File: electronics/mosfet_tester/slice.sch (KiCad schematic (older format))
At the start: 18 parts, among them J201 TEST_1P, J202 TEST_1P, J203 TEST_1P, J204 TEST_1P, J205 TEST_1P, J206 TEST_1P, J207 TEST_1P, Q201 Q_NMOS_GSD, U201 LM358

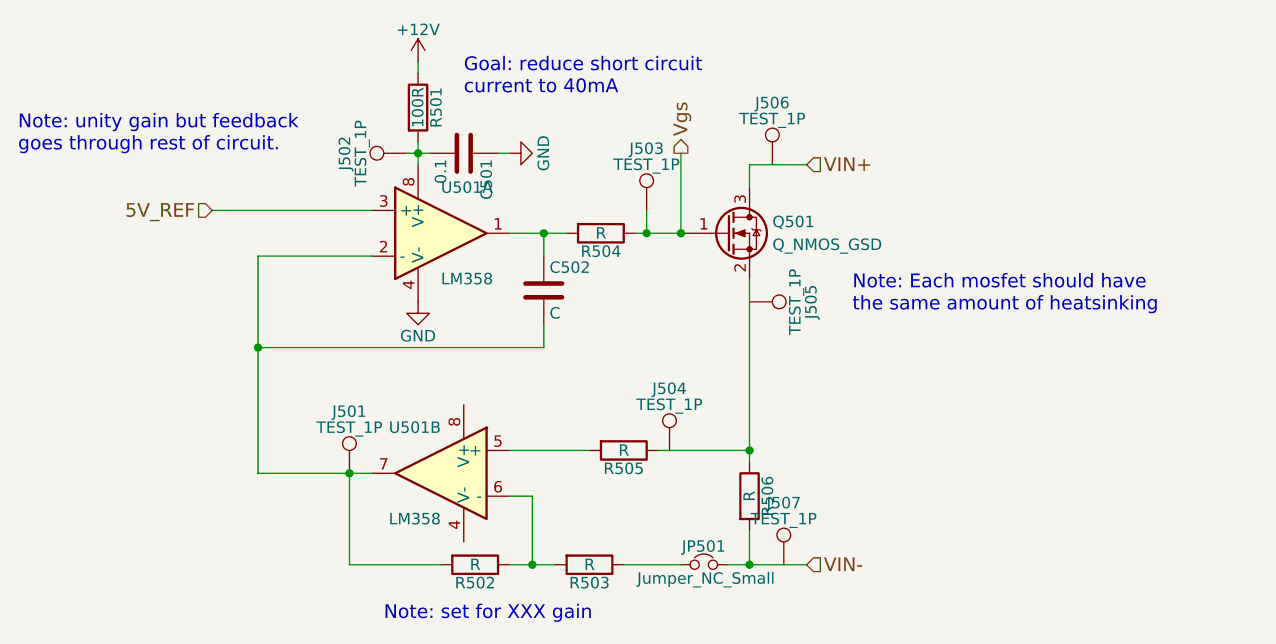
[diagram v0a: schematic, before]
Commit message: mosfet tester progress
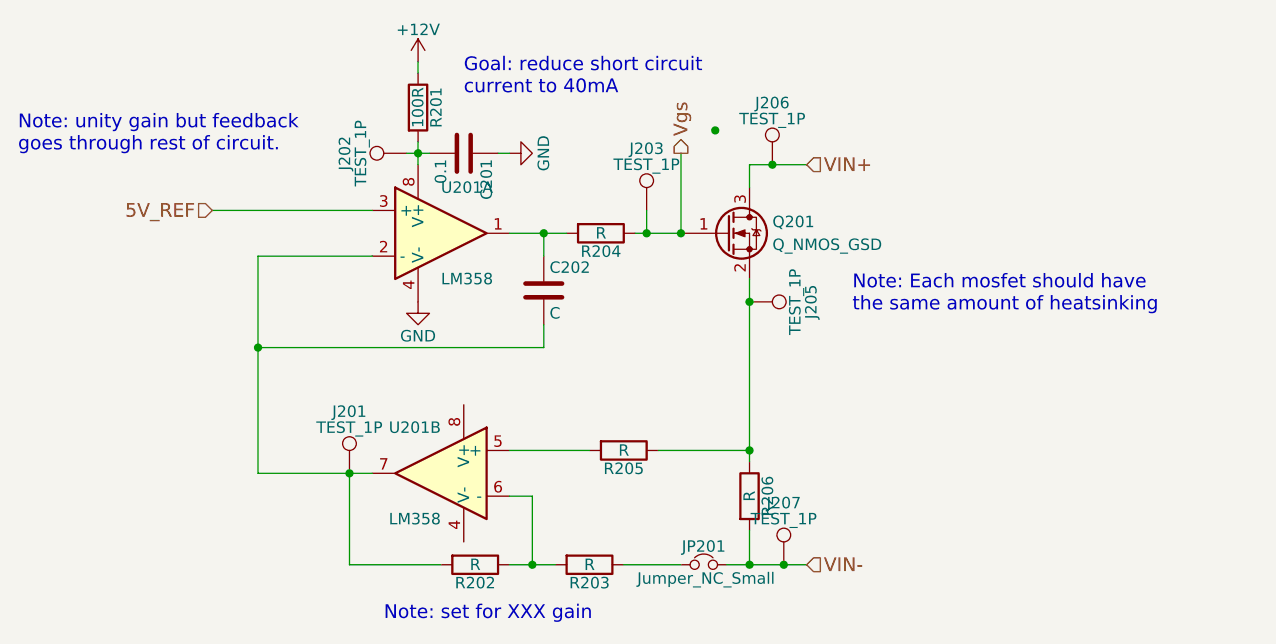
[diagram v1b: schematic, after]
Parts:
- removed J204: TEST_1P, Pin_Headers:Pin_Header_Straight_1x01_Pitch2.54mm, symbol TEST_1P
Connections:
- net VIN+: now also J206.1
- net VIN-: now also J207.1
- net at Q201.2 (S), R205.1, R206.1: now also J205.1
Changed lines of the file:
@@
 $Descr A4 11693 8268
 encoding utf-8
-Sheet 2 5
+Sheet 2 2
 Title ""
 Date ""
@@
 AR Path="/59556CE1/59553827" Ref="Q401"  Part="1"
 AR Path="/59557090/59553827" Ref="Q501"  Part="1"
-F 0 "Q501" H 4250 2350 50  0000 L CNN
+F 0 "Q201" H 4250 2350 50  0000 L CNN
 F 1 "Q_NMOS_GSD" H 4250 2250 50  0000 L CNN
 F 2 "TO_SOT_Packages_SMD:SOT-23_Handsoldering" H 4250 2400 50  0001 C CNN
@@
 AR Path="/59556CE1/5955382E" Ref="R406"  Part="1"
 AR Path="/59557090/5955382E" Ref="R506"  Part="1"
-F 0 "R506" V 4230 3450 50  0000 C CNN
+F 0 "R206" V 4230 3450 50  0000 C CNN
 F 1 "R" V 4150 3450 50  0000 C CNN
 F 2 "Resistors_SMD:R_2816_HandSoldering" V 4080 3450 50  0001 C CNN
@@
 AR Path="/59556CE1/59553867" Ref="U401"  Part="1"
 AR Path="/59557090/59553867" Ref="U501"  Part="1"
-F 0 "U501" H 2800 2500 50  0000 L CNN
+F 0 "U201" H 2800 2500 50  0000 L CNN
 F 1 "LM358" H 2800 2100 50  0000 L CNN
 F 2 "Housings_SOIC:SOIC-8_3.9x4.9mm_Pitch1.27mm" H 2800 2300 50  0001 C CNN
@@
 AR Path="/59556CE1/595538B8" Ref="U401"  Part="2"
 AR Path="/59557090/595538B8" Ref="U501"  Part="2"
-F 0 "U501" H 2800 3550 50  0000 L CNN
+F 0 "U201" H 2800 3550 50  0000 L CNN
 F 1 "LM358" H 2800 3150 50  0000 L CNN
 F 2 "Housings_SOIC:SOIC-8_3.9x4.9mm_Pitch1.27mm" H 2800 3350 50  0001 C CNN
@@
 Note: set for XXX gain
 $Comp
-L +12V #PWR201
+L +12V #PWR08
 U 1 1 59553CF4
 P 2700 1550
-AR Path="/595536CF/59553CF4" Ref="#PWR201"  Part="1"
+AR Path="/595536CF/59553CF4" Ref="#PWR08"  Part="1"
 AR Path="/59556746/59553CF4" Ref="#PWR301"  Part="1"
 AR Path="/59556CE1/59553CF4" Ref="#PWR401"  Part="1"
 AR Path="/59557090/59553CF4" Ref="#PWR501"  Part="1"
-F 0 "#PWR501" H 2700 1400 50  0001 C CNN
+F 0 "#PWR08" H 2700 1400 50  0001 C CNN
 F 1 "+12V" H 2700 1690 50  0000 C CNN
 F 2 "" H 2700 1550 50  0001 C CNN
@@
 AR Path="/59556CE1/59553D78" Ref="R401"  Part="1"
 AR Path="/59557090/59553D78" Ref="R501"  Part="1"
-F 0 "R501" V 2780 1750 50  0000 C CNN
+F 0 "R201" V 2780 1750 50  0000 C CNN
 F 1 "100R" V 2700 1750 50  0000 C CNN
 F 2 "Resistors_SMD:R_0603_HandSoldering" V 2630 1750 50  0001 C CNN
@@
 AR Path="/59556CE1/59553ED0" Ref="C401"  Part="1"
 AR Path="/59557090/59553ED0" Ref="C501"  Part="1"
-F 0 "C501" H 2925 2050 50  0000 L CNN
+F 0 "C201" H 2925 2050 50  0000 L CNN
 F 1 "0.1" H 2925 1850 50  0000 L CNN
 F 2 "Capacitors_SMD_Round:C_0603" H 2938 1800 50  0001 C CNN
@@
 	2700 1600 2700 1550
 $Comp
-L GND #PWR203
+L GND #PWR09
 U 1 1 59553F9C
 P 3100 1950
-AR Path="/595536CF/59553F9C" Ref="#PWR203"  Part="1"
+AR Path="/595536CF/59553F9C" Ref="#PWR09"  Part="1"
 AR Path="/59556746/59553F9C" Ref="#PWR303"  Part="1"
 AR Path="/59556CE1/59553F9C" Ref="#PWR403"  Part="1"
 AR Path="/59557090/59553F9C" Ref="#PWR503"  Part="1"
-F 0 "#PWR503" H 3100 1700 50  0001 C CNN
+F 0 "#PWR09" H 3100 1700 50  0001 C CNN
 F 1 "GND" H 3100 1800 50  0000 C CNN
 F 2 "" H 3100 1950 50  0001 C CNN
@@
 AR Path="/59556CE1/59554405" Ref="R405"  Part="1"
 AR Path="/59557090/59554405" Ref="R505"  Part="1"
-F 0 "R505" V 3680 3250 50  0000 C CNN
+F 0 "R205" V 3680 3250 50  0000 C CNN
 F 1 "R" V 3600 3250 50  0000 C CNN
 F 2 "Resistors_SMD:R_0603_HandSoldering" V 3530 3250 50  0001 C CNN
@@
 AR Path="/59556CE1/5955448A" Ref="R404"  Part="1"
 AR Path="/59557090/5955448A" Ref="R504"  Part="1"
-F 0 "R504" V 3580 2300 50  0000 C CNN
+F 0 "R204" V 3580 2300 50  0000 C CNN
 F 1 "R" V 3500 2300 50  0000 C CNN
 F 2 "Resistors_SMD:R_0603_HandSoldering" V 3430 2300 50  0001 C CNN
@@
 AR Path="/59556CE1/595544D0" Ref="C402"  Part="1"
 AR Path="/59557090/595544D0" Ref="C502"  Part="1"
-F 0 "C502" H 3275 2650 50  0000 L CNN
+F 0 "C202" H 3275 2650 50  0000 L CNN
 F 1 "C" H 3275 2450 50  0000 L CNN
 F 2 "Capacitors_SMD_Round:C_0603" H 3288 2400 50  0001 C CNN
@@
 AR Path="/59556CE1/5955455A" Ref="R403"  Part="1"
 AR Path="/59557090/5955455A" Ref="R503"  Part="1"
-F 0 "R503" V 3530 3750 50  0000 C CNN
+F 0 "R203" V 3530 3750 50  0000 C CNN
 F 1 "R" V 3450 3750 50  0000 C CNN
 F 2 "Resistors_SMD:R_0603_HandSoldering" V 3380 3750 50  0001 C CNN
@@
 AR Path="/59556CE1/5955458F" Ref="R402"  Part="1"
 AR Path="/59557090/5955458F" Ref="R502"  Part="1"
-F 0 "R502" V 3030 3750 50  0000 C CNN
+F 0 "R202" V 3030 3750 50  0000 C CNN
 F 1 "R" V 2950 3750 50  0000 C CNN
 F 2 "Resistors_SMD:R_0603_HandSoldering" V 2880 3750 50  0001 C CNN
@@
 AR Path="/59556CE1/59554722" Ref="JP401"  Part="1"
 AR Path="/59557090/59554722" Ref="JP501"  Part="1"
-F 0 "JP501" H 3950 3830 50  0000 C CNN
+F 0 "JP201" H 3950 3830 50  0000 C CNN
 F 1 "Jumper_NC_Small" H 3960 3690 50  0000 C CNN
 F 2 "SolderJumpers:SJ_1_NO" H 3950 3750 50  0001 C CNN
@@
 AR Path="/59556CE1/5955483A" Ref="J403"  Part="1"
 AR Path="/59557090/5955483A" Ref="J503"  Part="1"
-F 0 "J503" H 3700 2470 50  0000 C CNN
+F 0 "J203" H 3700 2470 50  0000 C CNN
 F 1 "TEST_1P" H 3700 2400 50  0000 C CNN
 F 2 "Pin_Headers:Pin_Header_Straight_1x01_Pitch2.54mm" H 3900 2200 50  0001 C CNN
 F 3 "" H 3900 2200 50  0001 C CNN
 	1    3700 2200
-	1    0    0    -1
-$EndComp
-$Comp
-L TEST_1P J204
-U 1 1 59554893
-P 3800 3250
-AR Path="/595536CF/59554893" Ref="J204"  Part="1"
-AR Path="/59556746/59554893" Ref="J304"  Part="1"
-AR Path="/59556CE1/59554893" Ref="J404"  Part="1"
-AR Path="/59557090/59554893" Ref="J504"  Part="1"
-F 0 "J504" H 3800 3520 50  0000 C CNN
-F 1 "TEST_1P" H 3800 3450 50  0000 C CNN
-F 2 "Pin_Headers:Pin_Header_Straight_1x01_Pitch2.54mm" H 4000 3250 50  0001 C CNN
-F 3 "" H 4000 3250 50  0001 C CNN
-	1    3800 3250
 	1    0    0    -1
 $EndComp
@@
 AR Path="/59556CE1/595548D4" Ref="J401"  Part="1"
 AR Path="/59557090/595548D4" Ref="J501"  Part="1"
-F 0 "J501" H 2400 3620 50  0000 C CNN
+F 0 "J201" H 2400 3620 50  0000 C CNN
 F 1 "TEST_1P" H 2400 3550 50  0000 C CNN
 F 2 "Pin_Headers:Pin_Header_Straight_1x01_Pitch2.54mm" H 2600 3350 50  0001 C CNN
@@
 AR Path="/59556CE1/5955497F" Ref="J406"  Part="1"
 AR Path="/59557090/5955497F" Ref="J506"  Part="1"
-F 0 "J506" H 4250 2270 50  0000 C CNN
+F 0 "J206" H 4250 2270 50  0000 C CNN
 F 1 "TEST_1P" H 4250 2200 50  0000 C CNN
 F 2 "Pin_Headers:Pin_Header_Straight_1x01_Pitch2.54mm" H 4450 2000 50  0001 C CNN
@@
 AR Path="/59556CE1/59554A4D" Ref="J407"  Part="1"
 AR Path="/59557090/59554A4D" Ref="J507"  Part="1"
-F 0 "J507" H 4300 4020 50  0000 C CNN
+F 0 "J207" H 4300 4020 50  0000 C CNN
 F 1 "TEST_1P" H 4300 3950 50  0000 C CNN
 F 2 "Pin_Headers:Pin_Header_Straight_1x01_Pitch2.54mm" H 4500 3750 50  0001 C CNN
@@
 AR Path="/59556CE1/59554AD6" Ref="J405"  Part="1"
 AR Path="/59557090/59554AD6" Ref="J505"  Part="1"
-F 0 "J505" H 4150 2870 50  0000 C CNN
+F 0 "J205" H 4150 2870 50  0000 C CNN
 F 1 "TEST_1P" H 4150 2800 50  0000 C CNN
 F 2 "Pin_Headers:Pin_Header_Straight_1x01_Pitch2.54mm" H 4350 2600 50  0001 C CNN
@@
 $EndComp
 $Comp
-L GND #PWR202
+L GND #PWR010
 U 1 1 59554C5F
 P 2700 2600
-AR Path="/595536CF/59554C5F" Ref="#PWR202"  Part="1"
+AR Path="/595536CF/59554C5F" Ref="#PWR010"  Part="1"
 AR Path="/59556746/59554C5F" Ref="#PWR302"  Part="1"
 AR Path="/59556CE1/59554C5F" Ref="#PWR402"  Part="1"
 AR Path="/59557090/59554C5F" Ref="#PWR502"  Part="1"
-F 0 "#PWR502" H 2700 2350 50  0001 C CNN
+F 0 "#PWR010" H 2700 2350 50  0001 C CNN
 F 1 "GND" H 2700 2450 50  0000 C CNN
 F 2 "" H 2700 2600 50  0001 C CNN
@@
 AR Path="/59556CE1/59555179" Ref="J402"  Part="1"
 AR Path="/59557090/59555179" Ref="J502"  Part="1"
-F 0 "J502" H 2650 2220 50  0000 C CNN
+F 0 "J202" H 2650 2220 50  0000 C CNN
 F 1 "TEST_1P" H 2650 2150 50  0000 C CNN
 F 2 "Pin_Headers:Pin_Header_Straight_1x01_Pitch2.54mm" H 2850 1950 50  0001 C CNN
@@
 	3850 2300 3850 1950
 Connection ~ 3850 2300
+Connection ~ 4300 3750
+Connection ~ 4250 2000
+Connection ~ 4150 2600
+Connection ~ 4000 1850
 $EndSCHEMATC

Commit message: Rework entire board, still in progress
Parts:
- removed J206, J207: TEST_1P, Pin_Headers:Pin_Header_Straight_1x01_Pitch2.54mm, symbol TEST_1P
- removed JP201: Jumper_NC_Small, SolderJumpers:SJ_1_NO, symbol Jumper_NC_Small
- Q201: footprint TO_SOT_Packages_SMD:SOT-23_Handsoldering -> TO_Combo_Packages:TO_220_247
- R204: renamed from R205; footprint Resistors_SMD:R_0603_HandSoldering -> Resistors_THT:R_Axial_DIN0207_L6.3mm_D2.5mm_P10.16mm_Horizontal
- R205: renamed from R204; footprint Resistors_SMD:R_0603_HandSoldering -> Resistors_THT:R_Axial_DIN0207_L6.3mm_D2.5mm_P10.16mm_Horizontal
- renumbered J205 to J204
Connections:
- net VIN-: now also R203.1
- net Vgs: now also C202.1, R205.2, U201.1; no longer Q201.1 (G), R205.1
- net at Q201.2 (S), R204.1, R206.1: no longer J204.1
- net at R204.2, U201.5 (+): now also J204.1
- new net: Q201.1 (G), R205.1
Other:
- moved on the sheet: J203, J204, R204, R205

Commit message: Checkpoint mosfet tester
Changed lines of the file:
@@
 LIBS:valves
 LIBS:zeropin
+LIBS:buckmodule
 LIBS:mosfet_tester-cache
 EELAYER 25 0
@@
 AR Path="/59812351/5955382E" Ref="R406"  Part="1"
 AR Path="/59812983/5955382E" Ref="R506"  Part="1"
-F 0 "R206" V 4230 3450 50  0000 C CNN
+F 0 "R506" V 4230 3450 50  0000 C CNN
 F 1 "R" V 4150 3450 50  0000 C CNN
 F 2 "Resistors_SMD:R_2816_HandSoldering" V 4080 3450 50  0001 C CNN
@@
 AR Path="/59812351/59553867" Ref="U401"  Part="1"
 AR Path="/59812983/59553867" Ref="U501"  Part="1"
-F 0 "U201" H 2800 2500 50  0000 L CNN
+F 0 "U501" H 2800 2500 50  0000 L CNN
 F 1 "LM358" H 2800 2100 50  0000 L CNN
 F 2 "Housings_SOIC:SOIC-8_3.9x4.9mm_Pitch1.27mm" H 2800 2300 50  0001 C CNN
@@
 AR Path="/59812351/595538B8" Ref="U401"  Part="2"
 AR Path="/59812983/595538B8" Ref="U501"  Part="2"
-F 0 "U201" H 2800 3550 50  0000 L CNN
+F 0 "U501" H 2800 3550 50  0000 L CNN
 F 1 "LM358" H 2800 3150 50  0000 L CNN
 F 2 "Housings_SOIC:SOIC-8_3.9x4.9mm_Pitch1.27mm" H 2800 3350 50  0001 C CNN
@@
 Note: set for XXX gain
 $Comp
-L +12V #PWR011
+L +12V #PWR10
 U 1 1 59553CF4
 P 2700 1550
-AR Path="/595536CF/59553CF4" Ref="#PWR011"  Part="1"
-AR Path="/59811E07/59553CF4" Ref="#PWR014"  Part="1"
-AR Path="/59812351/59553CF4" Ref="#PWR017"  Part="1"
-AR Path="/59812983/59553CF4" Ref="#PWR020"  Part="1"
-F 0 "#PWR011" H 2700 1400 50  0001 C CNN
+AR Path="/595536CF/59553CF4" Ref="#PWR10"  Part="1"
+AR Path="/59811E07/59553CF4" Ref="#PWR13"  Part="1"
+AR Path="/59812351/59553CF4" Ref="#PWR16"  Part="1"
+AR Path="/59812983/59553CF4" Ref="#PWR19"  Part="1"
+F 0 "#PWR19" H 2700 1400 50  0001 C CNN
 F 1 "+12V" H 2700 1690 50  0000 C CNN
 F 2 "" H 2700 1550 50  0001 C CNN
@@
 AR Path="/59812351/59553D78" Ref="R401"  Part="1"
 AR Path="/59812983/59553D78" Ref="R501"  Part="1"
-F 0 "R201" V 2780 1750 50  0000 C CNN
+F 0 "R501" V 2780 1750 50  0000 C CNN
 F 1 "100R" V 2700 1750 50  0000 C CNN
 F 2 "Resistors_SMD:R_0603_HandSoldering" V 2630 1750 50  0001 C CNN
@@
 AR Path="/59812351/59553ED0" Ref="C401"  Part="1"
 AR Path="/59812983/59553ED0" Ref="C501"  Part="1"
-F 0 "C201" H 2925 2050 50  0000 L CNN
+F 0 "C501" H 2925 2050 50  0000 L CNN
 F 1 "0.1" H 2925 1850 50  0000 L CNN
 F 2 "Capacitors_SMD_Round:C_0603" H 2938 1800 50  0001 C CNN
@@
 	2700 1600 2700 1550
 $Comp
-L GND #PWR012
+L GND #PWR12
 U 1 1 59553F9C
 P 3100 1950
-AR Path="/595536CF/59553F9C" Ref="#PWR012"  Part="1"
-AR Path="/59811E07/59553F9C" Ref="#PWR015"  Part="1"
-AR Path="/59812351/59553F9C" Ref="#PWR018"  Part="1"
-AR Path="/59812983/59553F9C" Ref="#PWR021"  Part="1"
-F 0 "#PWR012" H 3100 1700 50  0001 C CNN
+AR Path="/595536CF/59553F9C" Ref="#PWR12"  Part="1"
+AR Path="/59811E07/59553F9C" Ref="#PWR15"  Part="1"
+AR Path="/59812351/59553F9C" Ref="#PWR18"  Part="1"
+AR Path="/59812983/59553F9C" Ref="#PWR21"  Part="1"
+F 0 "#PWR21" H 3100 1700 50  0001 C CNN
 F 1 "GND" H 3100 1800 50  0000 C CNN
 F 2 "" H 3100 1950 50  0001 C CNN
@@
 AR Path="/59812351/59554405" Ref="R404"  Part="1"
 AR Path="/59812983/59554405" Ref="R504"  Part="1"
-F 0 "R204" V 3830 3250 50  0000 C CNN
+F 0 "R504" V 3830 3250 50  0000 C CNN
 F 1 "R" V 3750 3250 50  0000 C CNN
 F 2 "Resistors_THT:R_Axial_DIN0207_L6.3mm_D2.5mm_P10.16mm_Horizontal" V 3680 3250 50  0001 C CNN
@@
 AR Path="/59812351/5955448A" Ref="R405"  Part="1"
 AR Path="/59812983/5955448A" Ref="R505"  Part="1"
-F 0 "R205" V 3780 2300 50  0000 C CNN
+F 0 "R505" V 3780 2300 50  0000 C CNN
 F 1 "R" V 3700 2300 50  0000 C CNN
 F 2 "Resistors_THT:R_Axial_DIN0207_L6.3mm_D2.5mm_P10.16mm_Horizontal" V 3630 2300 50  0001 C CNN
@@
 AR Path="/59812351/595544D0" Ref="C402"  Part="1"
 AR Path="/59812983/595544D0" Ref="C502"  Part="1"
-F 0 "C202" H 3275 2650 50  0000 L CNN
+F 0 "C502" H 3275 2650 50  0000 L CNN
 F 1 "C" H 3275 2450 50  0000 L CNN
 F 2 "Capacitors_SMD_Round:C_0603" H 3288 2400 50  0001 C CNN
@@
 AR Path="/59812351/5955455A" Ref="R403"  Part="1"
 AR Path="/59812983/5955455A" Ref="R503"  Part="1"
-F 0 "R203" V 3530 3750 50  0000 C CNN
+F 0 "R503" V 3530 3750 50  0000 C CNN
 F 1 "R" V 3450 3750 50  0000 C CNN
 F 2 "Resistors_SMD:R_0603_HandSoldering" V 3380 3750 50  0001 C CNN
@@
 AR Path="/59812351/5955458F" Ref="R402"  Part="1"
 AR Path="/59812983/5955458F" Ref="R502"  Part="1"
-F 0 "R202" V 3030 3750 50  0000 C CNN
+F 0 "R502" V 3030 3750 50  0000 C CNN
 F 1 "R" V 2950 3750 50  0000 C CNN
 F 2 "Resistors_SMD:R_0603_HandSoldering" V 2880 3750 50  0001 C CNN
@@
 AR Path="/59812351/5955483A" Ref="J403"  Part="1"
 AR Path="/59812983/5955483A" Ref="J503"  Part="1"
-F 0 "J203" H 3400 2470 50  0000 C CNN
+F 0 "J503" H 3400 2470 50  0000 C CNN
 F 1 "TEST_1P" H 3400 2400 50  0000 C CNN
 F 2 "Pin_Headers:Pin_Header_Straight_1x01_Pitch2.54mm" H 3600 2200 50  0001 C CNN
@@
 AR Path="/59812351/595548D4" Ref="J401"  Part="1"
 AR Path="/59812983/595548D4" Ref="J501"  Part="1"
-F 0 "J201" H 2400 3620 50  0000 C CNN
+F 0 "J501" H 2400 3620 50  0000 C CNN
 F 1 "TEST_1P" H 2400 3550 50  0000 C CNN
 F 2 "Pin_Headers:Pin_Header_Straight_1x01_Pitch2.54mm" H 2600 3350 50  0001 C CNN
@@
 AR Path="/59812351/59554AD6" Ref="J404"  Part="1"
 AR Path="/59812983/59554AD6" Ref="J504"  Part="1"
-F 0 "J204" H 3350 3470 50  0000 C CNN
+F 0 "J504" H 3350 3470 50  0000 C CNN
 F 1 "TEST_1P" H 3350 3400 50  0000 C CNN
 F 2 "Pin_Headers:Pin_Header_Straight_1x01_Pitch2.54mm" H 3550 3200 50  0001 C CNN
@@
 $EndComp
 $Comp
-L GND #PWR013
+L GND #PWR11
 U 1 1 59554C5F
 P 2700 2600
-AR Path="/595536CF/59554C5F" Ref="#PWR013"  Part="1"
-AR Path="/59811E07/59554C5F" Ref="#PWR016"  Part="1"
-AR Path="/59812351/59554C5F" Ref="#PWR019"  Part="1"
-AR Path="/59812983/59554C5F" Ref="#PWR022"  Part="1"
-F 0 "#PWR013" H 2700 2350 50  0001 C CNN
+AR Path="/595536CF/59554C5F" Ref="#PWR11"  Part="1"
+AR Path="/59811E07/59554C5F" Ref="#PWR14"  Part="1"
+AR Path="/59812351/59554C5F" Ref="#PWR17"  Part="1"
+AR Path="/59812983/59554C5F" Ref="#PWR20"  Part="1"
+F 0 "#PWR20" H 2700 2350 50  0001 C CNN
 F 1 "GND" H 2700 2450 50  0000 C CNN
 F 2 "" H 2700 2600 50  0001 C CNN
@@
 AR Path="/59812351/59555179" Ref="J402"  Part="1"
 AR Path="/59812983/59555179" Ref="J502"  Part="1"
-F 0 "J202" H 2650 2220 50  0000 C CNN
+F 0 "J502" H 2650 2220 50  0000 C CNN
 F 1 "TEST_1P" H 2650 2150 50  0000 C CNN
 F 2 "Pin_Headers:Pin_Header_Straight_1x01_Pitch2.54mm" H 2850 1950 50  0001 C CNN
@@
 AR Path="/59812351/59553827" Ref="Q401"  Part="1"
 AR Path="/59812983/59553827" Ref="Q501"  Part="1"
-F 0 "Q201" H 4250 2350 50  0000 L CNN
+F 0 "Q501" H 4250 2350 50  0000 L CNN
 F 1 "Q_NMOS_GSD" H 4250 2250 50  0000 L CNN
 F 2 "TO_Combo_Packages:TO_220_247" H 4250 2400 50  0001 C CNN
